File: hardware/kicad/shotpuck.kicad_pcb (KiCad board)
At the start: 2 copper layers, 36 x 34.8 mm, 35 parts, among them J1 TYPE-C 6PFS 2JCB1.6-H6.7 IPX8, J2 SWD pads, Q1 DMN63D8LDW, Q2 DMN2004DWK, U1 BMD-340-A-R, U2 LSM6DSO32TR, U3 MCP73831T-2ACI/OT, U4 BQ29700DSER

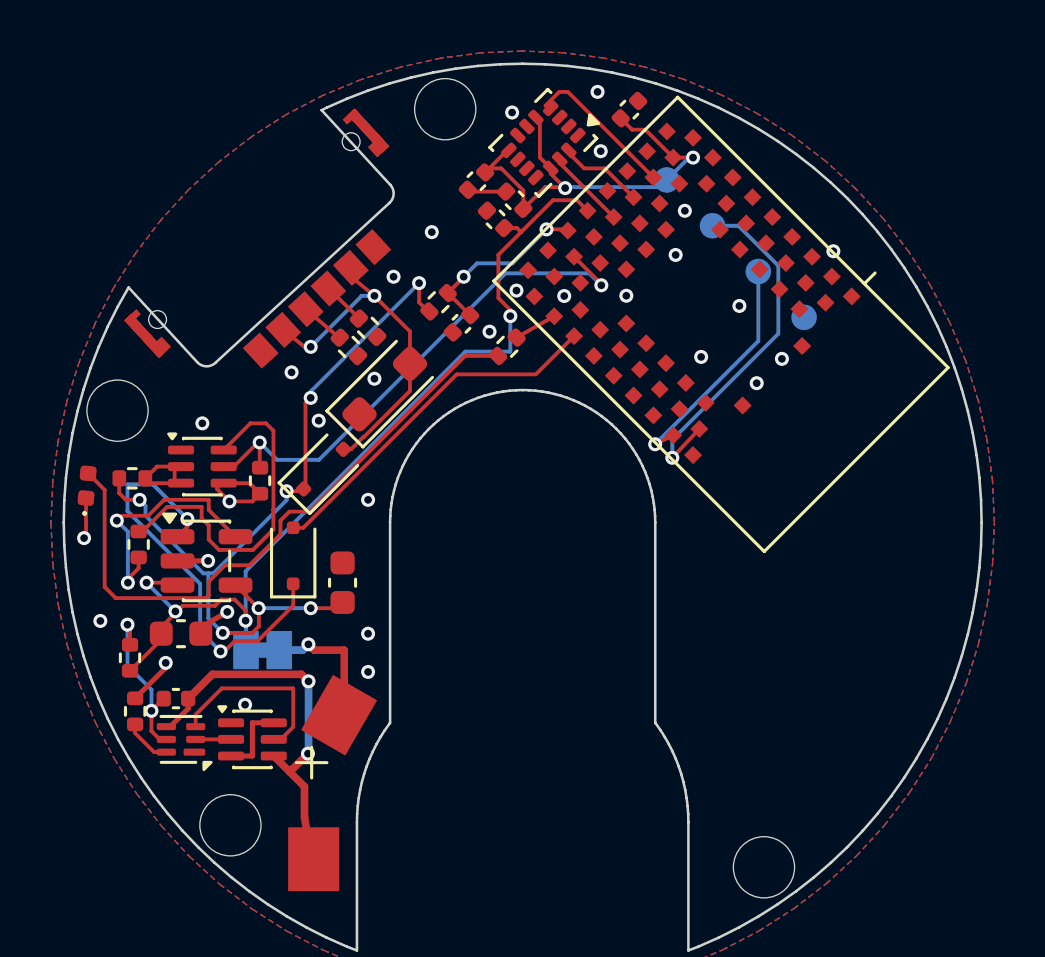
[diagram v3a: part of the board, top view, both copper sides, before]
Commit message: Add charger LED, JP2 reset pads and firmware recovery (0.2.1)
Charger LED: one blink every 2 s while charging, steady once the charger
has terminated (so the LED never holds off termination), three blinks
when the temperature gate pauses charging.

JP2: two bare round pads (0.8 mm, 0.4 mm gap) on module pin 7 (P0.26)
and GND. With the cap off, bridging them for 5 s erases settings,
pairings, shot count and log and reboots; only a bridge made while
running counts. Three crash or watchdog resets in a row, each within a
minute of boot, erase the same data automatically. A trial OTA image is
now confirmed only after a paired phone connects over an encrypted link.

Firmware rebuilt and signed as 0.2.1; panel gerbers and JLC BOM/CPL
regenerated (JP2 is copper only).

Co-Authored-By: Claude Opus 5.5 <noreply@anthropic.com>
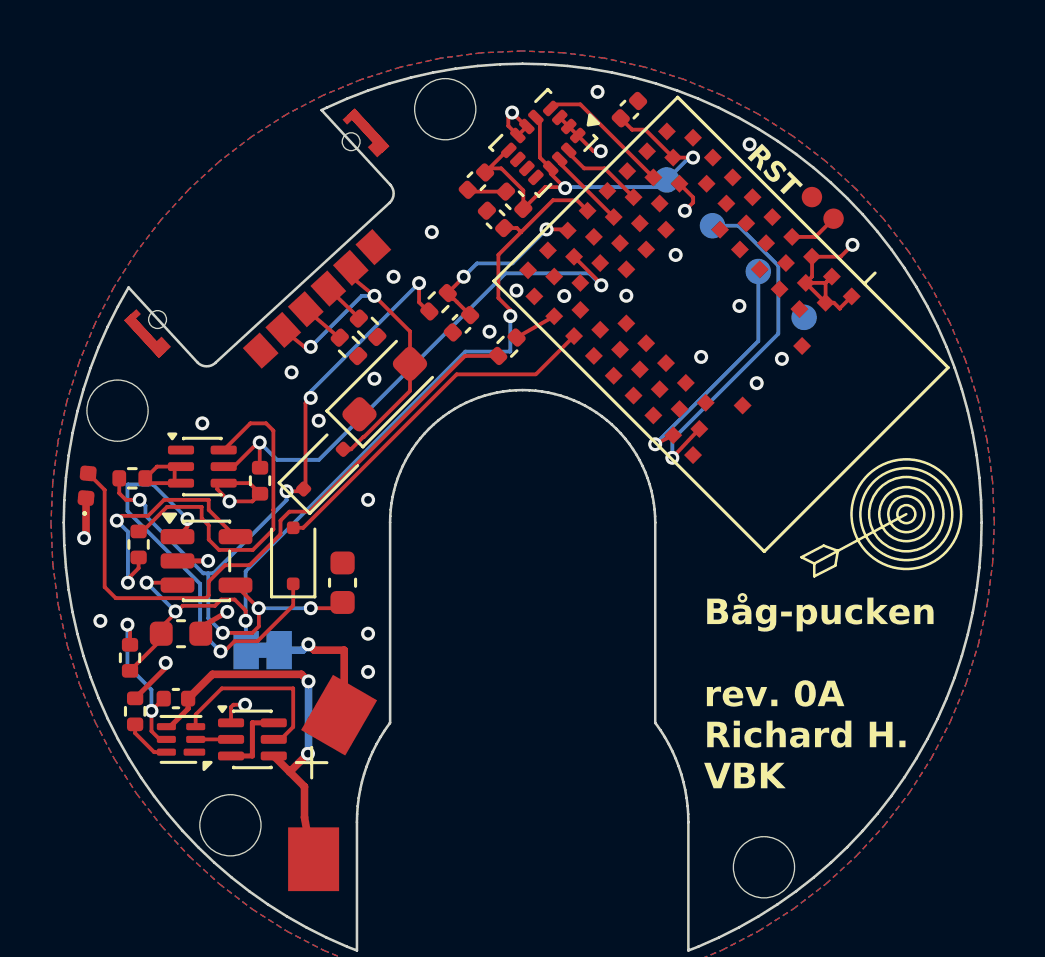
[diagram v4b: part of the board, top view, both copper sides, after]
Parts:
- added JP2: RESET pads, ShotPuck:TweezerPads_2x0.8mm_Gap0.4mm, F.Cu at (143.8, 79.0)
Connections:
- U1 pad 7: unconnected-(U1-P0.26-Pad7) -> /BTN
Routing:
- net /GND: track 11.4 -> 26.1 mm, vias 30 -> 31
- net /BTN: track 0.00 -> 1.92 mm
- net /ACC_INT1: track 5.85 -> 5.28 mm
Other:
- board text added: "Båg-pucken rev. 0A Richard H. VBK"
- board text added: "RST"

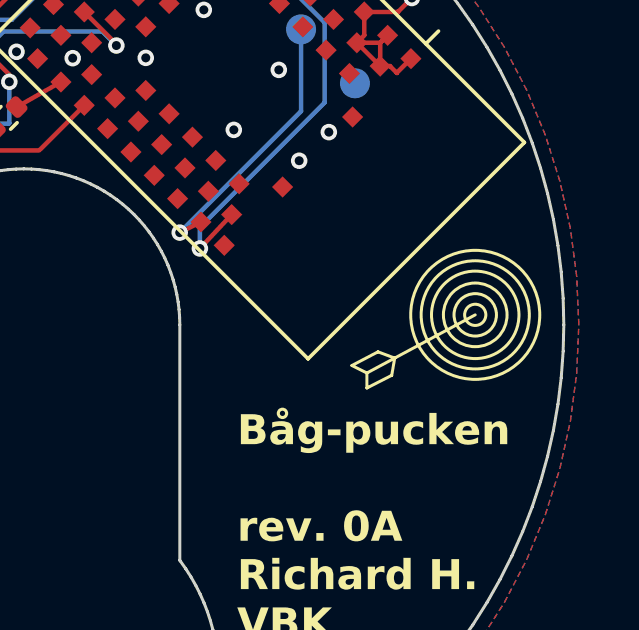
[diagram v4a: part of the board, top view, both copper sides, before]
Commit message: Update ShotPuck specifications and design files for USB-C integration
- Adjusted dimensions: puck diameter increased to Ø40 × 10.43 mm, with 1.6 mm free space above the cell.
- Updated IMU to ST LSM6DSO32XTR, reflecting changes in the BOM and design files.
- Revised PCB thickness from 0.8 mm to 1.2 mm, ensuring compatibility with new components.
- Enhanced layout.json and README.md to reflect the latest design specifications and assembly details.
- Removed obsolete components and updated the BOM for JLCPCB assembly.
- Regenerated fabrication files, including gerbers and BOM, to align with the latest design changes.

Co-Authored-By: Claude Opus 5.5 <noreply@anthropic.com>
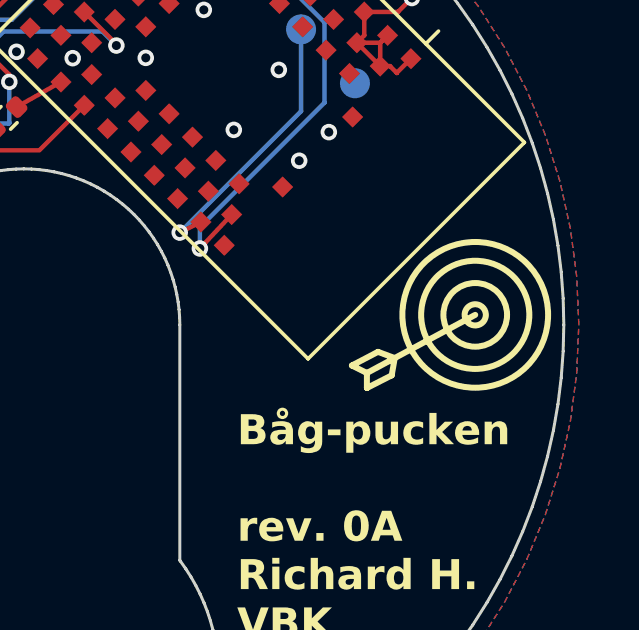
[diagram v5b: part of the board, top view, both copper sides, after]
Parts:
- U2: value LSM6DSO32TR -> LSM6DSO32XTR
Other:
- board text removed: "ShotPuck rev A"
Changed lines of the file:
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@@
 	(generator_version "10.0")
 	(general
-		(thickness 0.8)
+		(thickness 1.2)
 		(legacy_teardrops no)
 	)
@@
 		(fp_line
 			(start -0.3 0.25)
-			(end -0.299999 -0.25)
+			(end -0.299998 -0.25)
 			(stroke
 				(width 0.1)
@@
 			)
 		)
-		(property "Value" "LSM6DSO32TR"
+		(property "Value" "LSM6DSO32XTR"
 			(at 0 2.2 45)
 			(layer "F.Fab")
@@
 		(end 143.869556 92.294541)
 		(stroke
-			(width 0.1)
+			(width 0.2)
 			(type default)
 		)
@@
 		(end 143 92.75)
 		(stroke
-			(width 0.1)
+			(width 0.2)
 			(type default)
 		)
@@
 		(end 143.5 93.5)
 		(stroke
-			(width 0.1)
+			(width 0.2)
 			(type default)
 		)
@@
 		(end 147.111175 91.0614)
 		(stroke
-			(width 0.1)
+			(width 0.2)
 			(type default)
 		)
@@
 		(end 144.327352 93.078538)
 		(stroke
-			(width 0.1)
+			(width 0.2)
 			(type default)
 		)
@@
 		(end 144.427153 92.502273)
 		(stroke
-			(width 0.1)
+			(width 0.2)
 			(type default)
 		)
@@
 		(end 144.327352 93.078538)
 		(stroke
-			(width 0.1)
+			(width 0.2)
 			(type default)
 		)
@@
 		(end 147.361175 91.3114)
 		(stroke
-			(width 0.1)
-			(type default)
-		)
-		(fill no)
-		(layer "F.SilkS")
-	)
-	(gr_circle
-		(center 147.111175 91.0614)
-		(end 147.611175 91.5614)
-		(stroke
-			(width 0.1)
+			(width 0.2)
 			(type default)
 		)
@@
 		(end 147.861175 91.8114)
 		(stroke
-			(width 0.1)
-			(type default)
-		)
-		(fill no)
-		(layer "F.SilkS")
-	)
-	(gr_circle
-		(center 147.111175 91.0614)
-		(end 148.361175 91.8114)
-		(stroke
-			(width 0.1)
+			(width 0.2)
 			(type default)
 		)
@@
 		(end 148.611175 92.0614)
 		(stroke
-			(width 0.1)
+			(width 0.2)
 			(type default)
 		)
@@
 	(gr_circle
 		(center 147.111175 91.0614)
-		(end 148.861175 92.3114)
+		(end 149.5 91.5)
 		(stroke
-			(width 0.1)
+			(width 0.2)
 			(type default)
 		)
@@
 		)
 	)
-	(gr_text "ShotPuck rev A"
-		(at 11 6 0)
-		(layer "B.SilkS")
-		(effects
-			(font
-				(size 1 1)
-			)
-			(justify mirror)
-		)
-	)

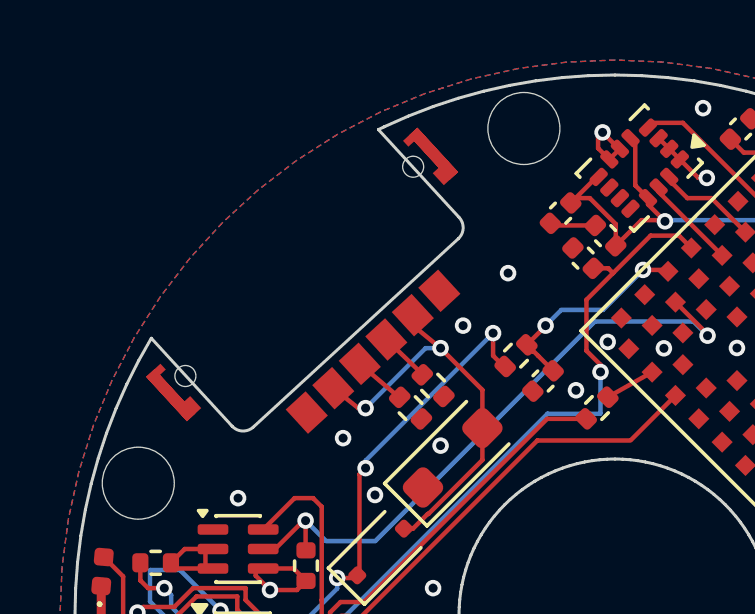
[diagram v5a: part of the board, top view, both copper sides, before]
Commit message: Update HANDOVER and README for recent design changes
- Enhanced J1's wing-tab pads for USB-C, increasing their area for better soldering.
- Adjusted D3's orientation in the CPL to match JLC's numbering.
- Added order package details in README for JLCPCB, including ORDER.md for order settings and checks.
- Regenerated fabrication files to reflect the latest design updates.

Co-Authored-By: Claude Opus 5.5 <noreply@anthropic.com>
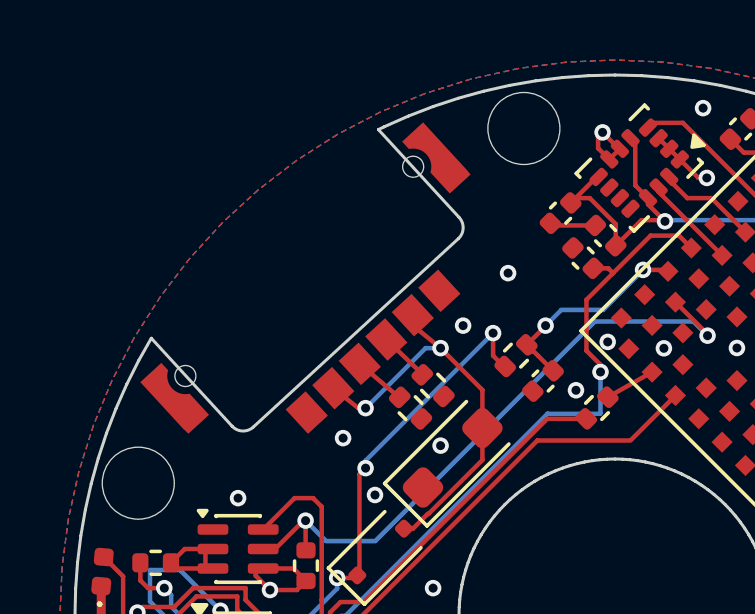
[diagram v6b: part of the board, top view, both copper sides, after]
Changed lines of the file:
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@@
 		(pad "SH" smd custom
 			(at -5.9475 1.595 222.5756807)
-			(size 0.385 2.01)
+			(size 0.2 0.2)
 			(layers "F.Cu" "F.Mask" "F.Paste")
 			(net "/GND")
@@
 				(gr_poly
 					(pts
-						(xy 0.4575 -1.005) (xy -0.1925 -1.005) (xy -0.1925 1.005) (xy 0.4575 1.005) (xy 0.4575 0.74) (xy 0.1925 0.74)
-						(xy 0.1925 -0.46) (xy 0.4575 -0.46)
+						(xy -0.4413 -1.345) (xy -0.449 -1.188) (xy -0.4525 -1.1643) (xy -0.4525 1.005) (xy 0.4975 1.005)
+						(xy 0.4975 0.6677) (xy 0.4564 0.643) (xy 0.4087 0.6077) (xy 0.3647 0.5678) (xy 0.3248 0.5238)
+						(xy 0.2895 0.4761) (xy 0.2589 0.4252) (xy 0.2336 0.3715) (xy 0.2136 0.3156) (xy 0.1991 0.258)
+						(xy 0.1904 0.1993) (xy 0.1875 0.14) (xy 0.1904 0.0807) (xy 0.1991 0.022) (xy 0.2136 -0.0356) (xy 0.2336 -0.0915)
+						(xy 0.2589 -0.1452) (xy 0.2895 -0.1961) (xy 0.3248 -0.2438) (xy 0.3647 -0.2878) (xy 0.4087 -0.3277)
+						(xy 0.4564 -0.363) (xy 0.4975 -0.3877) (xy 0.4975 -1.345)
 					)
 					(width 0)
@@
 		(pad "SH" smd custom
 			(at 5.947499 1.595 222.5756807)
-			(size 0.385 2.01)
+			(size 0.2 0.2)
 			(layers "F.Cu" "F.Mask" "F.Paste")
 			(net "/GND")
@@
 				(gr_poly
 					(pts
-						(xy -0.4575 -1.005) (xy 0.1925 -1.005) (xy 0.1925 1.005) (xy -0.4575 1.005) (xy -0.4575 0.74)
-						(xy -0.1925 0.74) (xy -0.1925 -0.46) (xy -0.4575 -0.46)
+						(xy 0.4525 1.005) (xy 0.4525 -1.1323) (xy 0.4428 -1.1979) (xy 0.4355 -1.345) (xy -0.4975 -1.345)
+						(xy -0.4975 -0.3877) (xy -0.4564 -0.363) (xy -0.4087 -0.3277) (xy -0.3647 -0.2878) (xy -0.3248 -0.2438)
+						(xy -0.2895 -0.1961) (xy -0.2589 -0.1452) (xy -0.2336 -0.0915) (xy -0.2136 -0.0356) (xy -0.1991 0.022)
+						(xy -0.1904 0.0807) (xy -0.1875 0.14) (xy -0.1904 0.1993) (xy -0.1991 0.258) (xy -0.2136 0.3156)
+						(xy -0.2336 0.3715) (xy -0.2589 0.4252) (xy -0.2895 0.4761) (xy -0.3248 0.5238) (xy -0.3647 0.5678)
+						(xy -0.4087 0.6077) (xy -0.4564 0.643) (xy -0.4975 0.6677) (xy -0.4975 1.005)
 					)
 					(width 0)

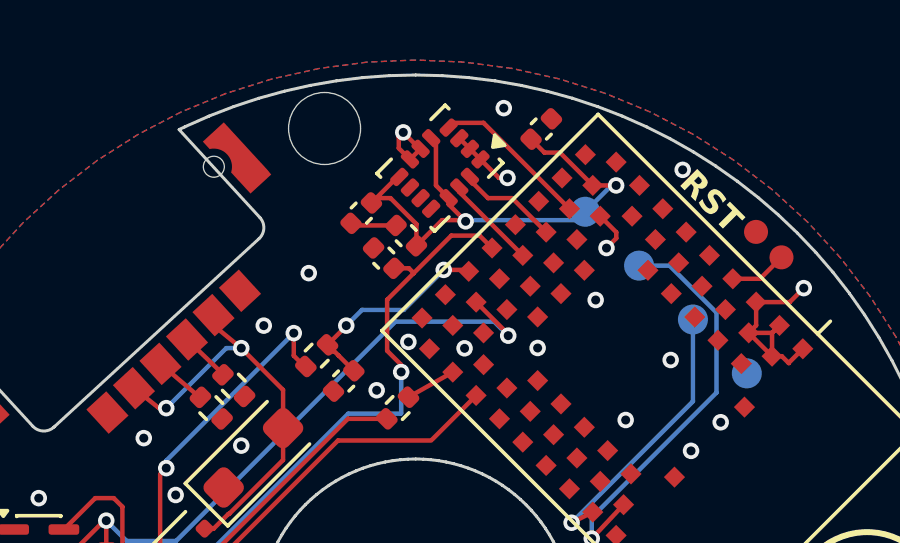
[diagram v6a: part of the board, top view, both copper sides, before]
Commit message: Update HANDOVER and README with design adjustments and fixes
- Adjusted panel fiducial positions and tooling hole sizes to meet JLCPCB specifications.
- Moved U2 and associated components inward for better clearance from the top tab.
- Fixed outline slivers in the panel design to resolve DRC issues, ensuring all runs pass.
- Regenerated fabrication files, including updated gerbers and BOM, to reflect the latest changes.

Co-Authored-By: Claude Opus 5.5 <noreply@anthropic.com>
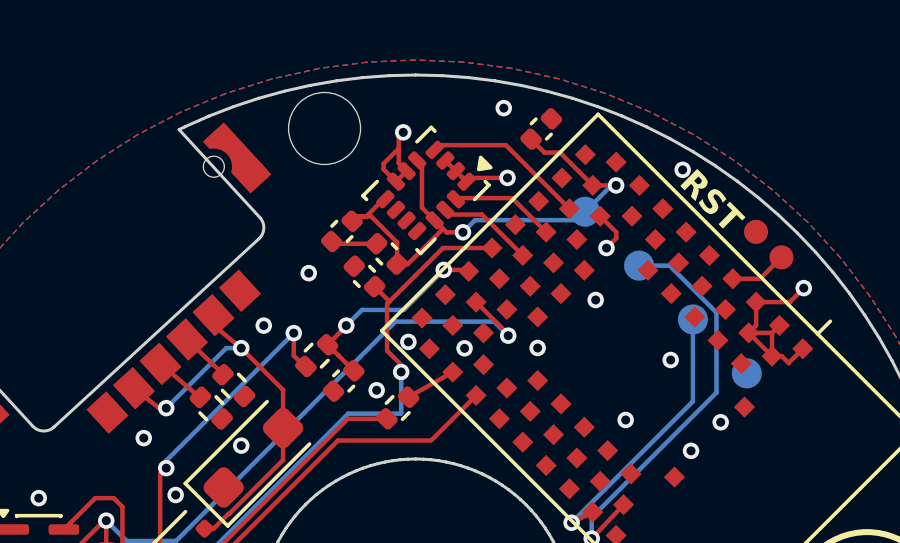
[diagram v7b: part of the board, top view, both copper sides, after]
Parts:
- moved C3 0.89 mm to (130.4, 80.1)
- moved C6 0.89 mm to (131.1, 79.4)
- moved C7 0.89 mm to (129.6, 78.6)
- moved U2 0.88 mm to (132.4, 77.2)
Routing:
- net /GND: track 26.1 -> 27.2 mm

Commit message: Switch U2 to LSM6DSV32XTR and assemble 4 boards
- U2 is the LSM6DSV32XTR (C22461202): same pinout and land pattern, JLC
  footprint within 0.013 mm at 0 deg. Value fields, BOMs, pos file and
  schematic PDF updated; gerbers, drill files and CPL rows unchanged.
  Board DRC 0/0 with 0 parity issues, panel DRC 0/0, ERC unchanged.
- Firmware 0.2.2: accel.c ported to the LSM6DSV32X register map. ACTIVE
  runs at 480 Hz (captures 720 samples, ring 1329, motion guard 10
  samples), IDLE at 15 Hz. Rebuilt shotpuck_full.hex and update.bin.
- Sim ground truth 3360 Hz (7 x 480 Hz); results.txt regenerated, PASS.
- JLC order: PCBA qty 2 panels, BOM/CPL for the bottom-row copies only
  (gen_jlc.py ASSEMBLED_COPIES), so 4 boards are assembled.
- README, HANDOVER, PROTOCOL, VALIDATION, ORDER.md and the order zip
  updated.

Co-Authored-By: Claude Opus 5.5 <noreply@anthropic.com>
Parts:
- U2: value LSM6DSO32XTR -> LSM6DSV32XTR
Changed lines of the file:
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@@
 			)
 		)
-		(property "Value" "LSM6DSO32XTR"
+		(property "Value" "LSM6DSV32XTR"
 			(at 0 2.2 45)
 			(layer "F.Fab")
